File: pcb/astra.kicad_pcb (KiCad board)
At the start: 4 copper layers, 49.2 x 45.5 mm, 89 parts, among them J1 Conn_01x02_Pin, J2 Conn_01x24_MountingPin, J3 Conn_02x04_Odd_Even, J4 Conn_02x05_Odd_Even, M1 Motor_DC, M2 Motor_DC, M3 Motor_DC, M4 Motor_DC, Q1 AO3400A, Q2 AO3400A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

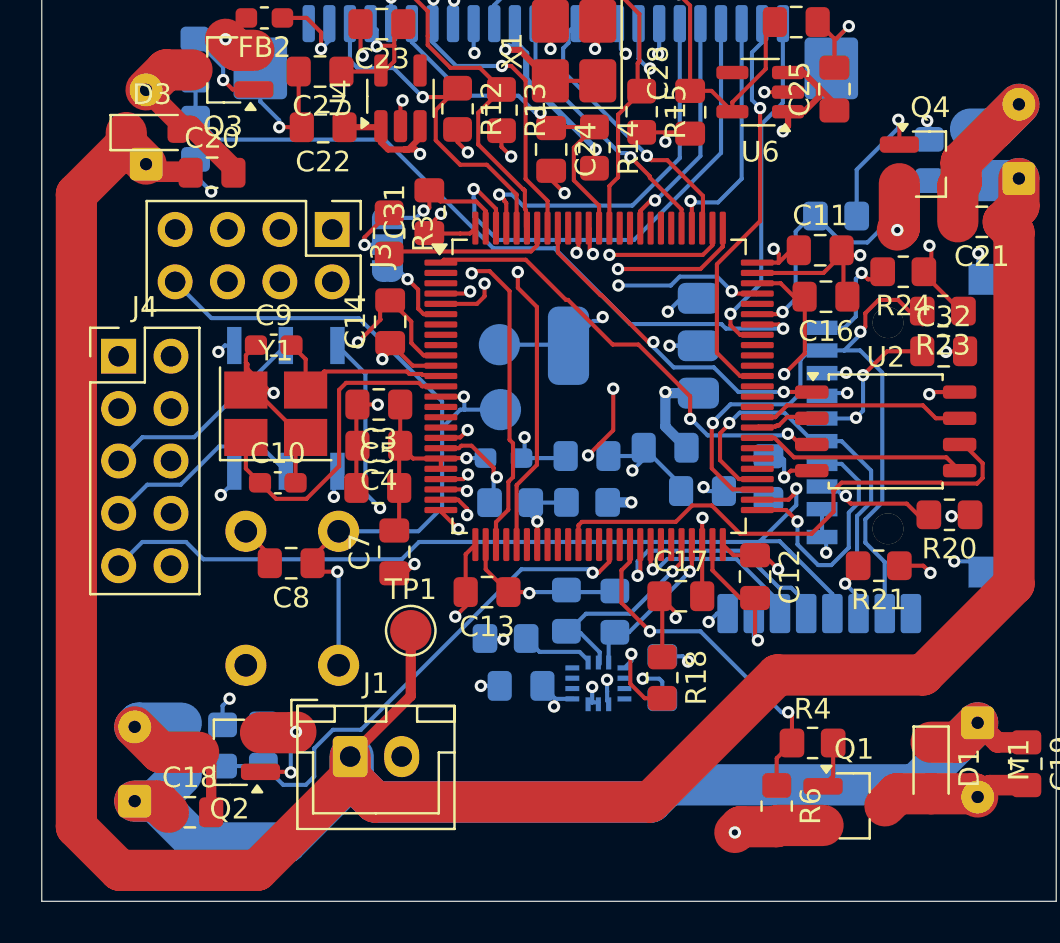
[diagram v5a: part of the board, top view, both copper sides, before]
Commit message: [pcb] add some 3d mooodels
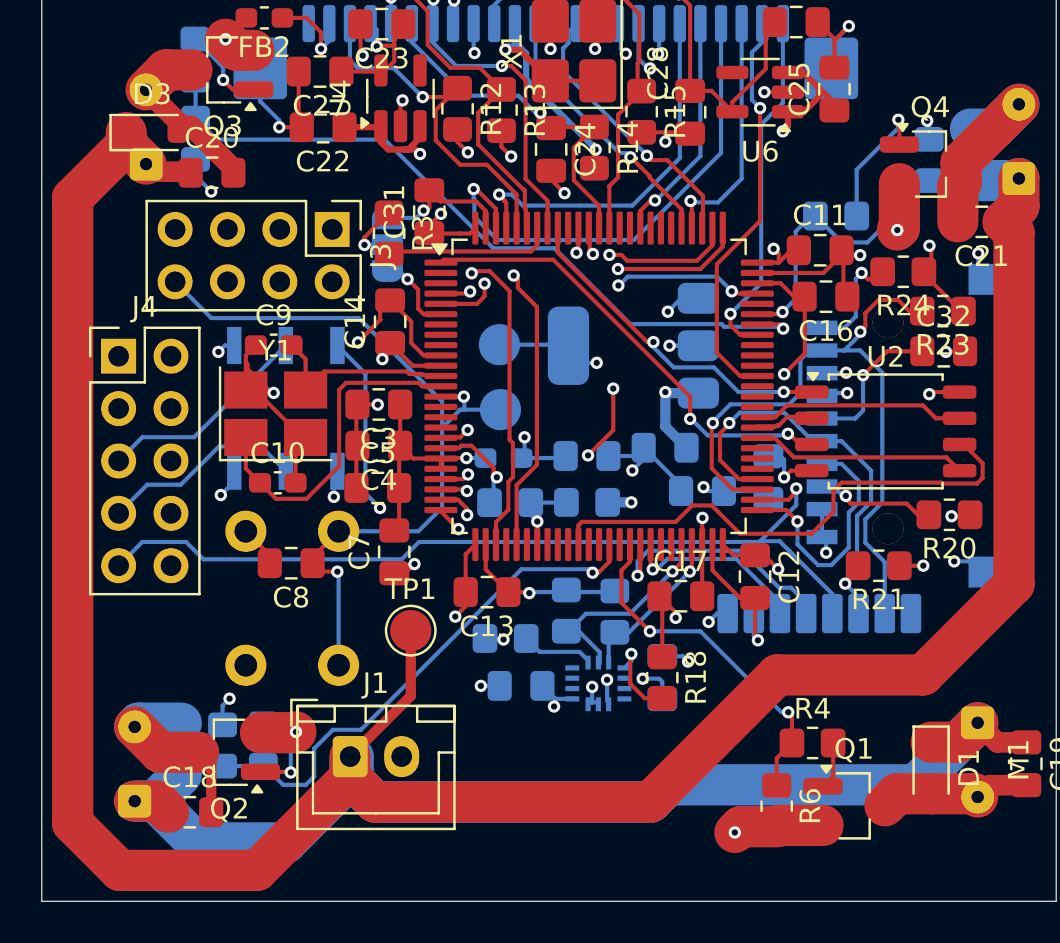
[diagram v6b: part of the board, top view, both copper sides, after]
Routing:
- net +3.3V: track 80.6 -> 79.6 mm, vias 25 -> 24

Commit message: [pcb] controller schematic, intial layout
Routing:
- net CS_SD: track 12.1 -> 9.11 mm
- net QSPI_CLK: track 25.5 -> 26.0 mm
- net GND: track 126.6 -> 126.4 mm, vias 38 -> 39

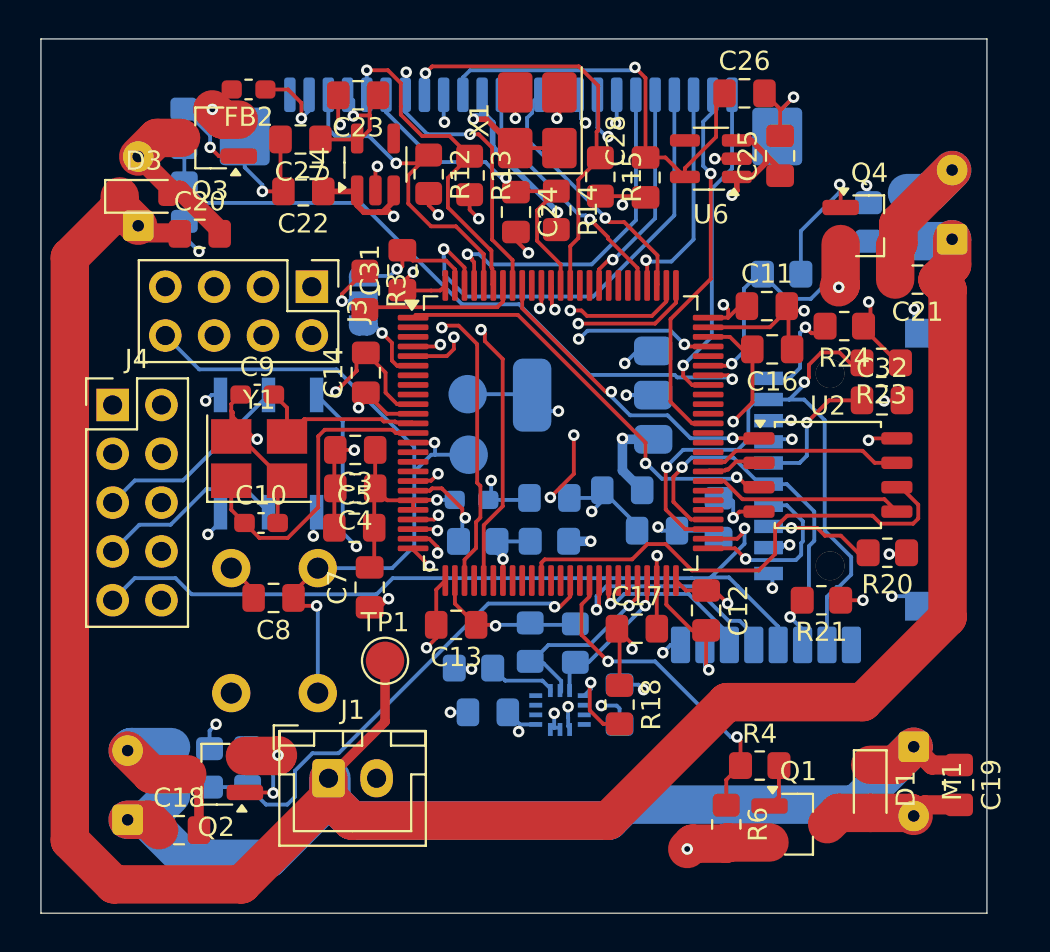
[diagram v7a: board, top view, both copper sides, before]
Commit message: [pcb] silkscreen labels and logos
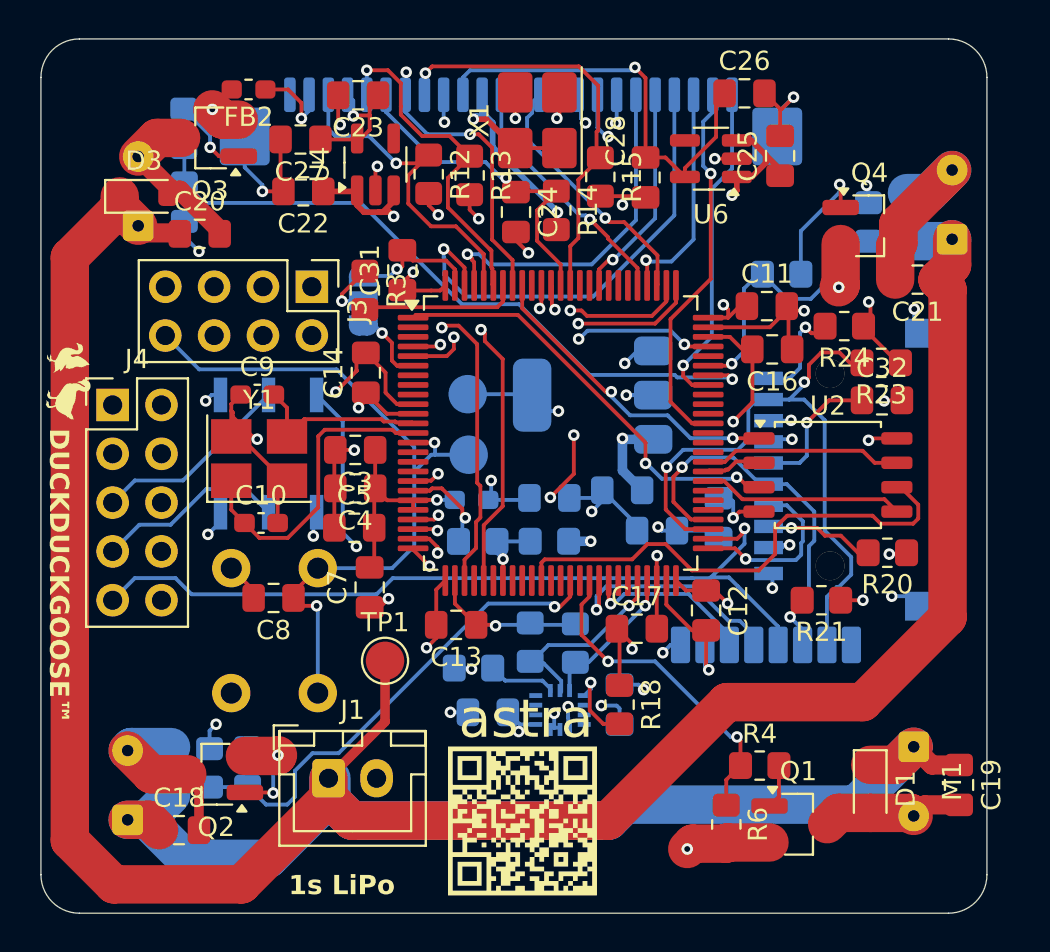
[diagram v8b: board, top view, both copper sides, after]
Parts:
- added G***: LOGO, LOGO, F.Cu at (119.0, 52.0)
- added G***: LOGO, LOGO, B.Cu at (141.0, 74.7)
- added G***: LOGO, LOGO, B.Cu at (152.8, 52.8)
- added QR*****: https://github.com/TheScientist101/astra, lcsc:qrcode, F.Cu at (142.7, 74.9)
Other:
- outline, holes or cut-outs redrawn
- board text added: "1s LiPo"
- board text added: "3V3"
- board text added: "DUCKDUCKGOOSE™"
- board text added: "I²C"
- board text added: "RESET"
- board text added: "RST"
- board text added: "SPI"
- board text added: "astra"
- board text added: "nRF24"
